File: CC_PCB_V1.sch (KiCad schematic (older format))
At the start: 6 parts, among them J2 Antenna_Conn_02x04_Odd_Even, J3 USB1130-15-A_REVA, J5 Relay_Conn_01x06, U1 Pico, U2 level_converter_BOB-12009

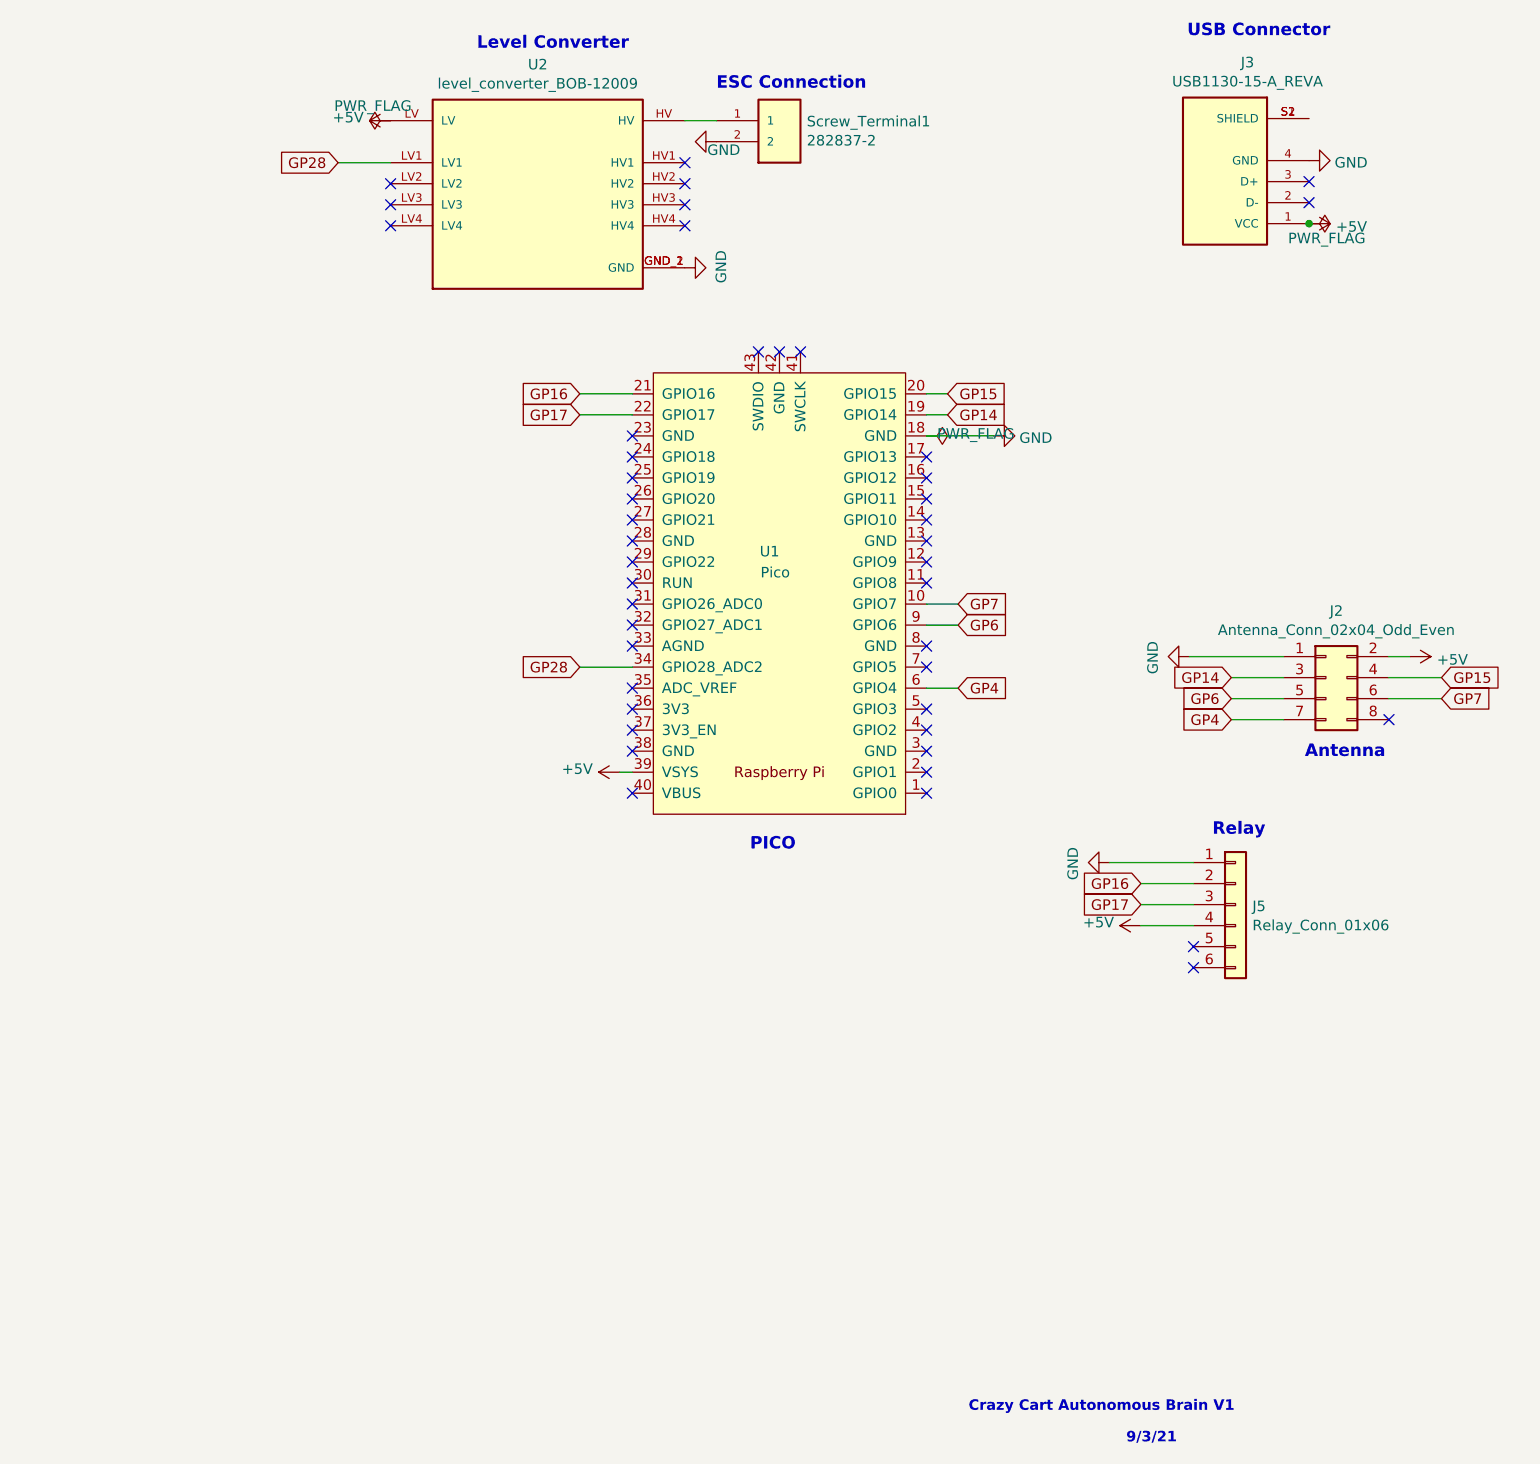
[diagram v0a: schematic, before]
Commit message: Version 2 of PCB
editing wiring, changing voltage regulator, and adding screw terminals.
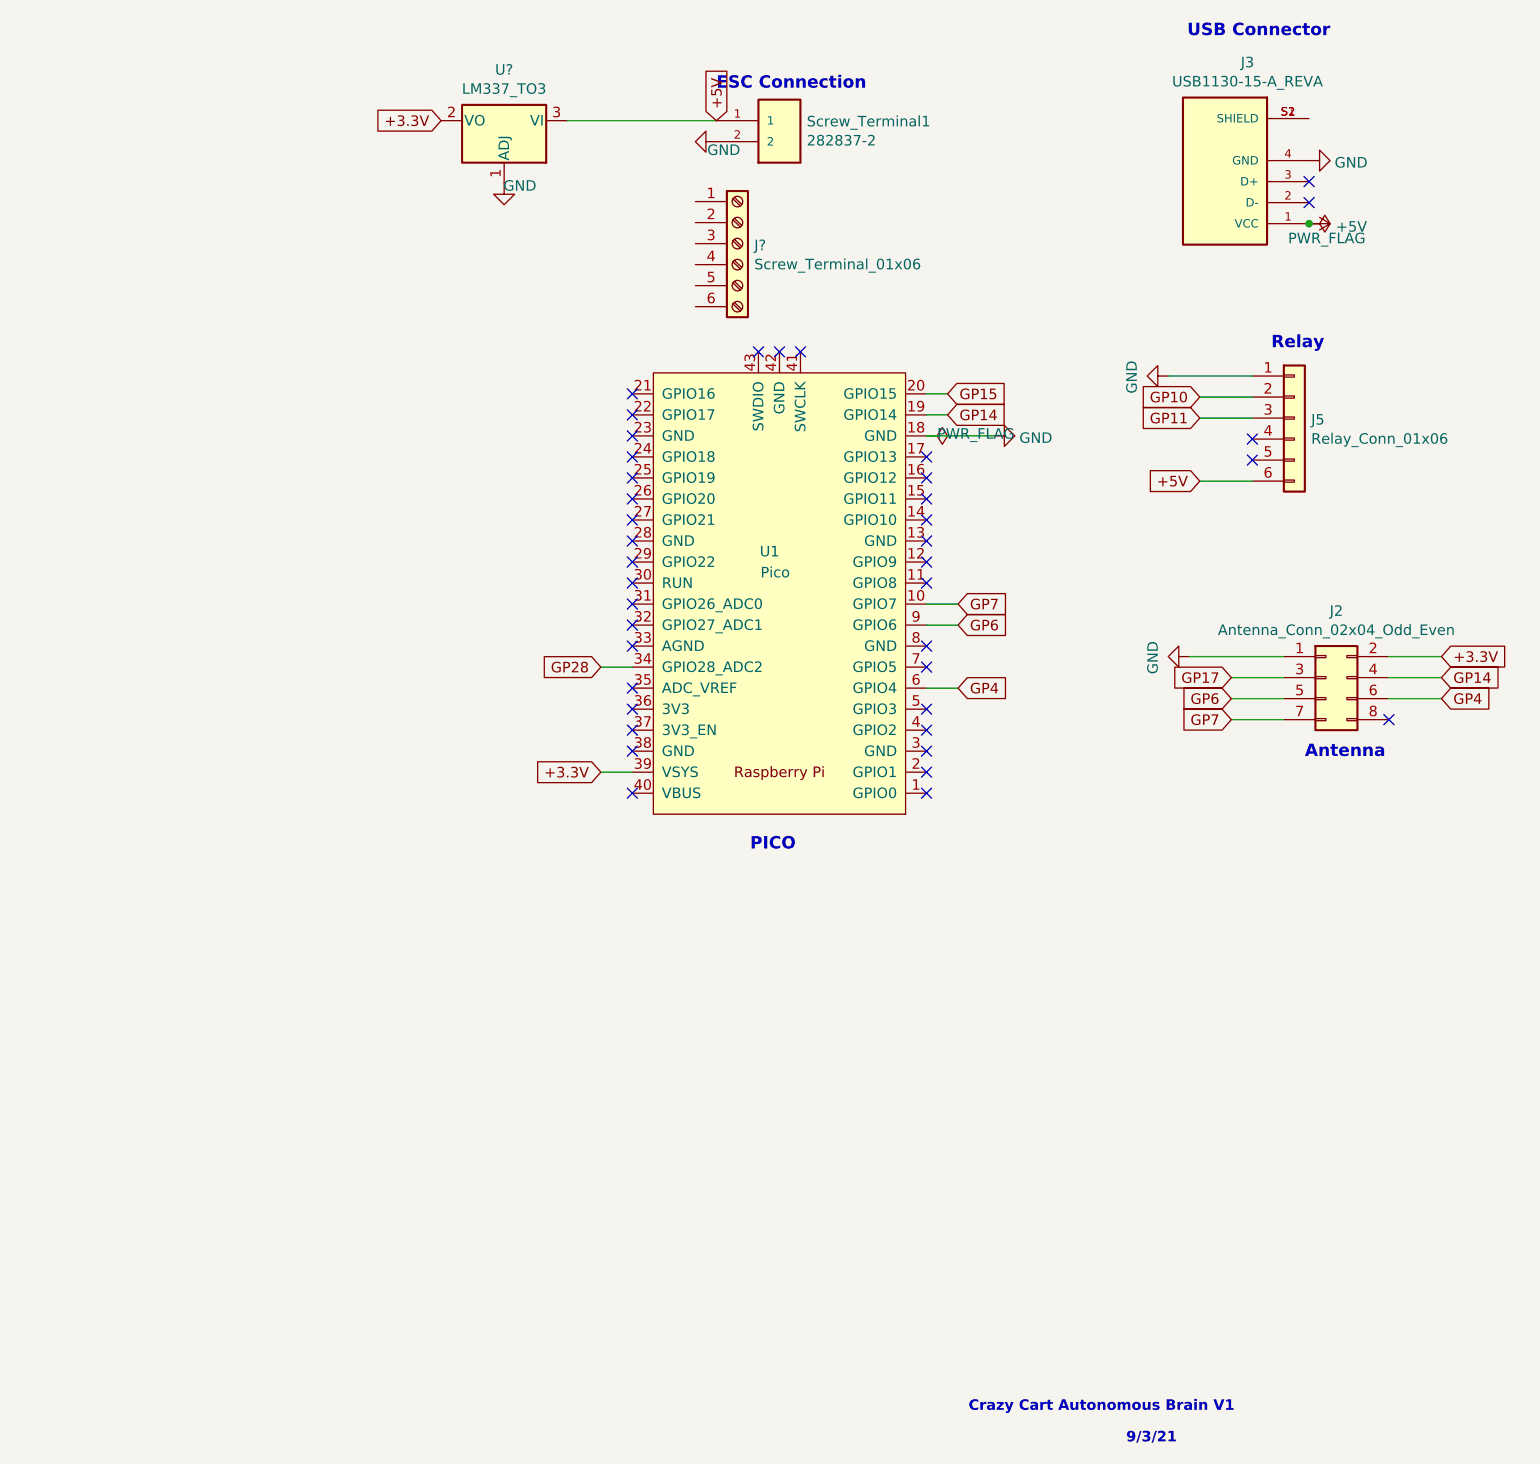
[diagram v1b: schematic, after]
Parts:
- removed U2: level_converter_BOB-12009, MCU_RaspberryPi_and_Boards:CONV_BOB-12009, symbol BOB-12009:BOB-12009
- added J?: Screw_Terminal_01x06, symbol Connector:Screw_Terminal_01x06
- added U?: LM337_TO3, Package_TO_SOT_THT:TO-3, symbol Regulator_Linear:LM337_TO3
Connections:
- net +5V: now also J5.6 (Pin_6), Screw_Terminal1.1, U?.3 (VI); no longer J2.2 (Pin_2), J5.4 (Pin_4), U1.39 (VSYS)
- net GND: now also U?.1 (ADJ)
- net GP14: now also J2.4 (Pin_4); no longer J2.3 (Pin_3)
- net GP15: no longer J2.4 (Pin_4)
- net GP17: now also J2.3 (Pin_3); no longer J5.3 (Pin_3), U1.22 (GPIO17)
- net GP4: now also J2.6 (Pin_6); no longer J2.7 (Pin_7)
- net GP7: now also J2.7 (Pin_7); no longer J2.6 (Pin_6)
- net GP16: no longer names the net of U1.21 (GPIO16)
- net GP16: no longer J5.2 (Pin_2)
- new net +3.3V: J2.2 (Pin_2), U1.39 (VSYS), U?.2 (VO)
- new net GP10: J5.2 (Pin_2)
- new net GP11: J5.3 (Pin_3)
- no-connect marks 45 -> 40
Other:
- note removed: "Level Converter"
- moved on the sheet: J5
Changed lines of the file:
@@
 L Connector_Generic:Conn_01x06 J5
 U 1 1 6132C346
-P 8620 5080
-F 0 "J5" H 8700 5072 50  0000 L CNN
-F 1 "Relay_Conn_01x06" H 8700 4981 50  0000 L CNN
-F 2 "Connector_PinHeader_2.00mm:PinHeader_1x06_P2.00mm_Vertical" H 8620 5080 50  0001 C CNN
-F 3 "~" H 8620 5080 50  0001 C CNN
-	1    8620 5080
+P 8900 2765
+F 0 "J5" H 8980 2757 50  0000 L CNN
+F 1 "Relay_Conn_01x06" H 8980 2666 50  0000 L CNN
+F 2 "Connector_PinHeader_2.00mm:PinHeader_1x06_P2.00mm_Vertical" H 8900 2765 50  0001 C CNN
+F 3 "~" H 8900 2765 50  0001 C CNN
+	1    8900 2765
 	1    0    0    -1
 $EndComp
@@
 	1    0    0    -1
 $EndComp
-Wire Wire Line
-	5500 3950 5750 3950
-Wire Wire Line
-	5500 2650 5750 2650
-Wire Wire Line
-	5500 2750 5750 2750
-Text GLabel 4350 1550 0    50   Input ~ 0
-GP28
 Text GLabel 9600 4000 2    50   Input ~ 0
-GP15
-Text GLabel 8600 4000 0    50   Input ~ 0
 GP14
 Text GLabel 7250 2750 2    50   Input ~ 0
 GP14
-Text GLabel 8170 4980 0    50   Input ~ 0
-GP16
-Text GLabel 8170 5080 0    50   Input ~ 0
+Text GLabel 8600 4000 0    50   Input ~ 0
 GP17
 Wire Wire Line
-	8170 4980 8420 4980
-Wire Wire Line
-	8170 5080 8420 5080
+	8450 2665 8700 2665
+Wire Wire Line
+	8450 2765 8700 2765
 Wire Wire Line
 	9350 4000 9600 4000
@@
 Wire Wire Line
 	7150 2750 7250 2750
-Wire Wire Line
-	4350 1550 4600 1550
-$Comp
-L BOB-12009:BOB-12009 U2
-U 1 1 61335072
-P 5300 1650
-F 0 "U2" H 5300 2217 50  0000 C CNN
-F 1 "level_converter_BOB-12009" H 5300 2126 50  0000 C CNN
-F 2 "MCU_RaspberryPi_and_Boards:CONV_BOB-12009" H 5300 1650 50  0001 L BNN
-F 3 "" H 5300 1650 50  0001 L BNN
-F 4 "N/A" H 5300 1650 50  0001 L BNN "MAXIMUM_PACKAGE_HEIGHT"
-F 5 "SparkFun Electronics" H 5300 1650 50  0001 L BNN "MANUFACTURER"
-F 6 "01" H 5300 1650 50  0001 L BNN "PARTREV"
-F 7 "Manufacturer Recommendations" H 5300 1650 50  0001 L BNN "STANDARD"
-	1    5300 1650
-	1    0    0    -1
-$EndComp
 $Comp
 L power:GND #PWR0102
@@
 Text GLabel 8600 4100 0    50   Input ~ 0
 GP6
-Text GLabel 9600 4100 2    50   Input ~ 0
+Text GLabel 8600 4200 0    50   Input ~ 0
 GP7
 Wire Wire Line
@@
 Wire Wire Line
 	8850 4100 8600 4100
-Wire Wire Line
-	7300 3650 7150 3650
 Wire Wire Line
 	7150 3750 7300 3750
@@
 L power:GND #PWR0105
 U 1 1 613C4FFD
-P 8020 4880
-F 0 "#PWR0105" H 8020 4630 50  0001 C CNN
-F 1 "GND" H 8025 4707 50  0000 C CNN
-F 2 "" H 8020 4880 50  0001 C CNN
-F 3 "" H 8020 4880 50  0001 C CNN
-	1    8020 4880
-	0    1    1    0
-$EndComp
-Wire Wire Line
-	8420 4880 8020 4880
-Wire Wire Line
-	8420 5180 8170 5180
-Text GLabel 8600 4200 0    50   Input ~ 0
+P 8300 2565
+F 0 "#PWR0105" H 8300 2315 50  0001 C CNN
+F 1 "GND" H 8305 2392 50  0000 C CNN
+F 2 "" H 8300 2565 50  0001 C CNN
+F 3 "" H 8300 2565 50  0001 C CNN
+	1    8300 2565
+	0    1    1    0
+$EndComp
+Wire Wire Line
+	8700 2565 8300 2565
+Wire Wire Line
+	8700 3065 8450 3065
+Text GLabel 9600 4100 2    50   Input ~ 0
 GP4
 Text Notes 8100 7650 0    50   ~ 10
@@
 NoConn ~ 6450 2450
 NoConn ~ 6550 2450
-NoConn ~ 4600 1850
-NoConn ~ 4600 1750
-NoConn ~ 4600 1650
-NoConn ~ 6000 1850
-NoConn ~ 6000 1650
-NoConn ~ 6000 1750
-NoConn ~ 6000 1550
 NoConn ~ 9350 4200
-NoConn ~ 8420 5280
-NoConn ~ 8420 5380
-$Comp
-L power:+5V #PWR0111
-U 1 1 6140F10C
-P 8170 5180
-F 0 "#PWR0111" H 8170 5030 50  0001 C CNN
-F 1 "+5V" V 8185 5308 50  0000 L CNN
-F 2 "" H 8170 5180 50  0001 C CNN
-F 3 "" H 8170 5180 50  0001 C CNN
-	1    8170 5180
-	0    -1   -1   0
-$EndComp
+NoConn ~ 8700 2965
+NoConn ~ 8700 2865
 $Comp
 L power:+5V #PWR0113
@@
 Text Notes 8950 4390 0    59   ~ 12
 Antenna
-Text Notes 8510 4760 0    59   ~ 12
+Text Notes 8790 2445 0    59   ~ 12
 Relay
 Text Notes 6310 4830 0    59   ~ 12
 PICO
-Text Notes 5010 1020 0    59   ~ 12
-Level Converter
 Text Notes 8390 960  0    59   ~ 12
 USB Connector\n
@@
 Text GLabel 7250 2650 2    50   Input ~ 0
 GP15
-Text GLabel 5500 3950 0    50   Input ~ 0
+Text GLabel 5600 3950 0    50   Input ~ 0
 GP28
-Text GLabel 5500 2750 0    50   Input ~ 0
-GP17
-Text GLabel 5500 2650 0    50   Input ~ 0
-GP16
-Wire Wire Line
-	9350 3900 9450 3900
 $Comp
 L 282837-2:282837-2 Screw_Terminal1
@@
 	1    0    0    -1
 $EndComp
-$Comp
-L power:+5V #PWR0104
-U 1 1 613A9FB6
-P 5690 4450
-F 0 "#PWR0104" H 5690 4300 50  0001 C CNN
-F 1 "+5V" V 5705 4578 50  0000 L CNN
-F 2 "" H 5690 4450 50  0001 C CNN
-F 3 "" H 5690 4450 50  0001 C CNN
-	1    5690 4450
-	0    -1   -1   0
-$EndComp
 NoConn ~ 5750 4150
 $Comp
@@
 $EndComp
 Connection ~ 8970 1840
-Wire Wire Line
-	5750 4450 5690 4450
-$Comp
-L power:+5V #PWR0106
-U 1 1 6137FAD9
-P 4600 1350
-F 0 "#PWR0106" H 4600 1200 50  0001 C CNN
-F 1 "+5V" V 4615 1478 50  0000 L CNN
-F 2 "" H 4600 1350 50  0001 C CNN
-F 3 "" H 4600 1350 50  0001 C CNN
-	1    4600 1350
-	0    -1   -1   0
-$EndComp
-$Comp
-L power:PWR_FLAG #FLG0105
-U 1 1 61389C22
-P 4600 1350
-F 0 "#FLG0105" H 4600 1425 50  0001 C CNN
-F 1 "PWR_FLAG" V 4670 1250 50  0000 L CNN
-F 2 "" H 4600 1350 50  0001 C CNN
-F 3 "~" H 4600 1350 50  0001 C CNN
-	1    4600 1350
-	0    -1   -1   0
-$EndComp
-$Comp
-L power:GND #PWR0107
-U 1 1 6138B5C9
-P 6000 2050
-F 0 "#PWR0107" H 6000 1800 50  0001 C CNN
-F 1 "GND" H 6005 1877 50  0000 C CNN
-F 2 "" H 6000 2050 50  0001 C CNN
-F 3 "" H 6000 2050 50  0001 C CNN
-	1    6000 2050
-	0    -1   -1   0
-$EndComp
-$Comp
-L power:+5V #PWR0108
-U 1 1 6138D18B
-P 9450 3900
-F 0 "#PWR0108" H 9450 3750 50  0001 C CNN
-F 1 "+5V" V 9465 4028 50  0000 L CNN
-F 2 "" H 9450 3900 50  0001 C CNN
-F 3 "" H 9450 3900 50  0001 C CNN
-	1    9450 3900
-	0    1    1    0
-$EndComp
-Wire Wire Line
-	6000 1350 6150 1350
 $Comp
 L power:GND #PWR0109
@@
 	0    1    1    0
 $EndComp
+Text GLabel 5600 4450 0    50   Input ~ 0
++3.3V
+Text GLabel 8450 3065 0    50   Input ~ 0
++5V
+Wire Wire Line
+	9350 3900 9600 3900
+Text GLabel 9600 3900 2    50   Input ~ 0
++3.3V
+NoConn ~ 5750 2650
+NoConn ~ 5750 2750
+Text GLabel 8450 2665 0    50   Input ~ 0
+GP10
+Text GLabel 8450 2765 0    50   Input ~ 0
+GP11
+Wire Wire Line
+	7300 3650 7150 3650
+Wire Wire Line
+	5750 3950 5600 3950
+Wire Wire Line
+	5750 4450 5600 4450
+Text GLabel 6150 1350 1    50   Input ~ 0
++5V
+$Comp
+L Regulator_Linear:LM337_TO3 U?
+U 1 1 6146A6D0
+P 5140 1350
+F 0 "U?" H 5140 1108 50  0000 C CNN
+F 1 "LM337_TO3" H 5140 1199 50  0000 C CNN
+F 2 "Package_TO_SOT_THT:TO-3" H 5140 1150 50  0001 C CIN
+F 3 "http://www.ti.com/lit/ds/symlink/lm337-n.pdf" H 5140 1350 50  0001 C CNN
+	1    5140 1350
+	-1   0    0    1
+$EndComp
+Wire Wire Line
+	6150 1350 5440 1350
+Text GLabel 4840 1350 0    50   Input ~ 0
++3.3V
+$Comp
+L power:GND #PWR?
+U 1 1 6146C342
+P 5140 1650
+F 0 "#PWR?" H 5140 1400 50  0001 C CNN
+F 1 "GND" H 5215 1640 50  0000 C CNN
+F 2 "" H 5140 1650 50  0001 C CNN
+F 3 "" H 5140 1650 50  0001 C CNN
+	1    5140 1650
+	1    0    0    -1
+$EndComp
+$Comp
+L Connector:Screw_Terminal_01x06 J?
+U 1 1 61471123
+P 6250 1935
+F 0 "J?" H 6330 1927 50  0000 L CNN
+F 1 "Screw_Terminal_01x06" H 6330 1836 50  0000 L CNN
+F 2 "" H 6250 1935 50  0001 C CNN
+F 3 "~" H 6250 1935 50  0001 C CNN
+	1    6250 1935
+	1    0    0    -1
+$EndComp
 $EndSCHEMATC
